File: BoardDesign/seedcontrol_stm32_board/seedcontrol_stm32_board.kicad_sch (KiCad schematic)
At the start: 3 parts, among them U1 STM32F401CCUx

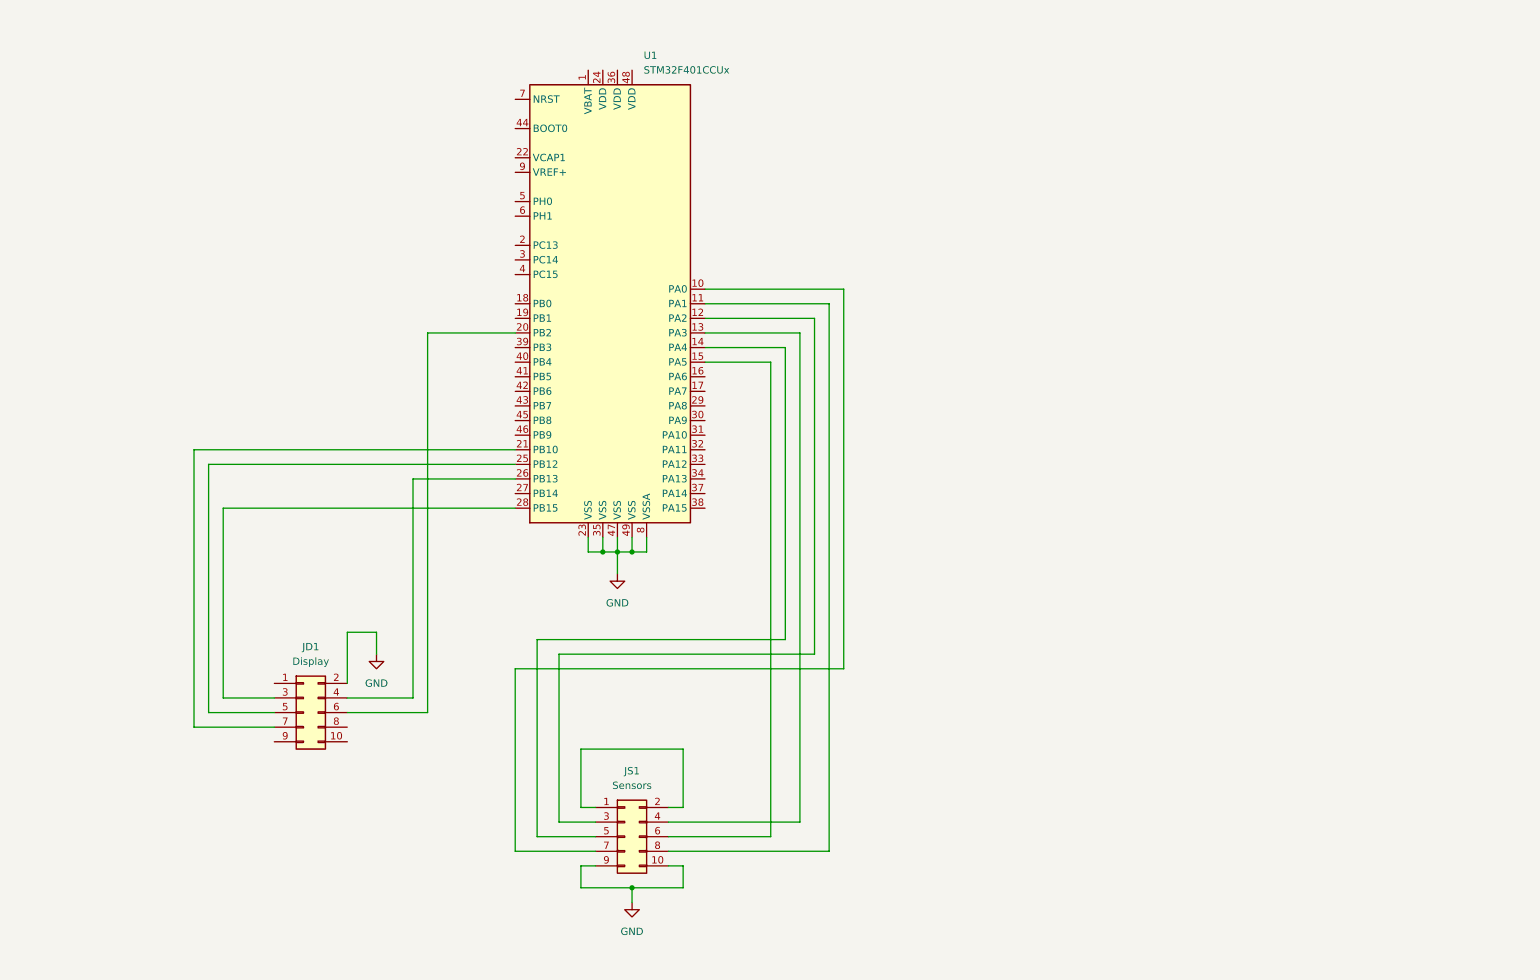
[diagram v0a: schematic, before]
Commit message: Added KiCAD schematic of the board and startet designing the PCB layout.
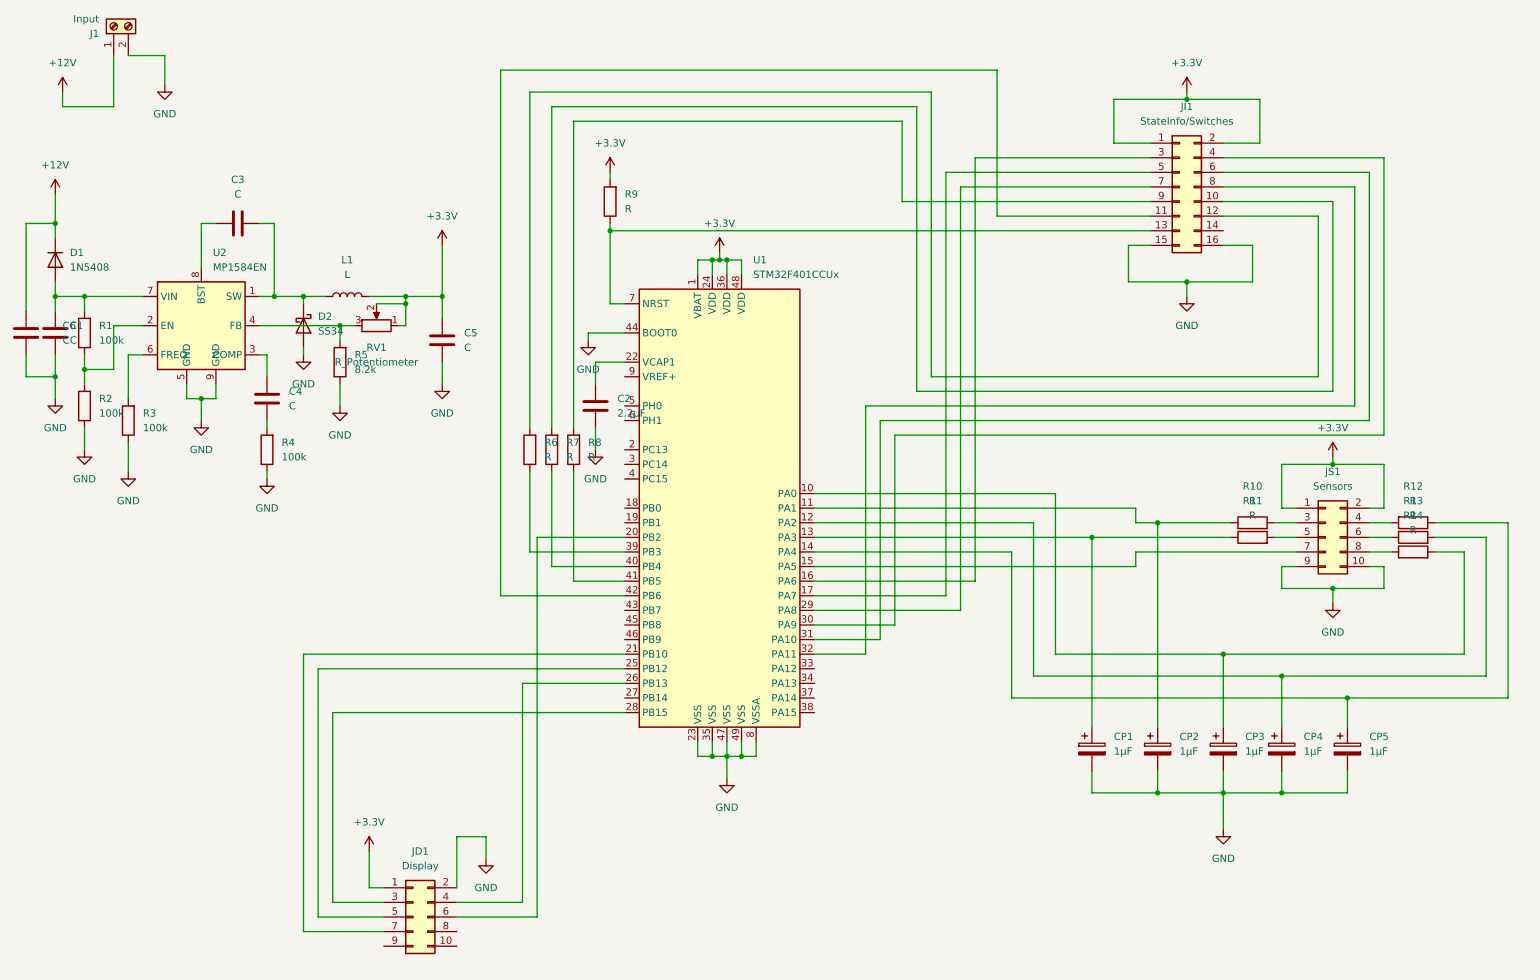
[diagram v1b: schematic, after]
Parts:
- added C1, C3, C4: C, Capacitor_SMD:C_0603_1608Metric, symbol Device:C
- added C2: 2.2µF, Capacitor_SMD:C_0402_1005Metric, symbol Device:C
- added C5, C6: C, Capacitor_SMD:C_1206_3216Metric, symbol Device:C
- added CP1, CP2, CP3, CP4, CP5: 1µF, Capacitor_THT:C_Rect_L10.0mm_W3.0mm_P7.50mm_MKS4, symbol Device:C_Polarized
- added D1: 1N5408, Diode_THT:D_DO-41_SOD81_P12.70mm_Horizontal, symbol Simulation_SPICE:DIODE
- added D2: SS34, Diode_SMD:D_SMC, symbol Device:D_Schottky
- added J1: Input, TerminalBlock:TerminalBlock_Altech_AK300-2_P5.00mm, symbol Connector:Screw_Terminal_01x02
- added JI1: StateInfo/Switches, Connector_PinHeader_2.54mm:PinHeader_2x08_P2.54mm_Vertical, symbol Connector_Generic:Conn_02x08_Odd_Even
- added L1: L, Inductor_SMD:L_Bourns_SRP7028A_7.3x6.6mm, symbol Device:L
- added R1, R2, R3, R4: 100k, Resistor_SMD:R_0603_1608Metric, symbol Device:R
- added R10, R11, R12, R13, R14: R, Resistor_THT:R_Axial_DIN0309_L9.0mm_D3.2mm_P12.70mm_Horizontal, symbol Device:R
- added R5: 8.2k, Resistor_SMD:R_0603_1608Metric, symbol Device:R
- added R6, R7, R8, R9: R, Resistor_SMD:R_0603_1608Metric, symbol Device:R
- added RV1: R_Potentiometer, Potentiometer_SMD:Potentiometer_Bourns_TC33X_Vertical, symbol Device_custom:R_Potentiometer
- added U2: MP1584EN, Package_SO:SOIC-8-1EP_3.9x4.9mm_P1.27mm_EP2.62x3.51mm, symbol Regulator_Switching_custom:MP1584EN
- JD1, JS1: footprint (none) -> Connector_PinHeader_2.54mm:PinHeader_2x05_P2.54mm_Vertical
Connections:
- net GND: now also U1.44 (BOOT0), C1.1, C2.1, C5.1, C6.1, CP1.2, CP2.2, CP3.2, CP4.2, CP5.2, D2.2 (A), J1.2 (Pin_2), JI1.15 (Pin_15), JI1.16 (Pin_16), R2.1, R3.1, R4.1, R5.1, U2.5 (GND), U2.9 (GND)
- net +3.3V: now reaches JS1.1 (Pin_1), JS1.2 (Pin_2)
- net +3.3V: now also JD1.1 (Pin_1), U1.1 (VBAT), U1.24 (VDD), U1.36 (VDD), U1.48 (VDD), C5.2, JI1.1 (Pin_1), JI1.2 (Pin_2), L1.2, R9.2, RV1.1, RV1.2
- net at U1.12 (PA2): now also CP4.1, R13.2; no longer JS1.3 (Pin_3)
- net at U1.13 (PA3): now also CP1.1, R11.1; no longer JS1.4 (Pin_4)
- net at JS1.5 (Pin_5): now also R11.2; no longer U1.14 (PA4)
- net at JS1.6 (Pin_6): now also R13.1; no longer U1.15 (PA5)
- net at U1.10 (PA0): now also CP3.1, R14.2; no longer JS1.7 (Pin_7)
- net at U1.11 (PA1): now also CP2.1, R10.1; no longer JS1.8 (Pin_8)
- net at U1.16 (PA6): now also JI1.3 (Pin_3)
- net at U1.17 (PA7): now also JI1.5 (Pin_5)
- net at U1.22 (VCAP1): now also C2.2
- net at U1.29 (PA8): now also JI1.7 (Pin_7)
- net at U1.30 (PA9): now also JI1.4 (Pin_4)
- net at U1.31 (PA10): now also JI1.6 (Pin_6)
- net at U1.32 (PA11): now also JI1.8 (Pin_8)
- net at U1.39 (PB3): now also R6.1
- net at U1.40 (PB4): now also R7.1
- net at U1.41 (PB5): now also R8.1
- net at U1.42 (PB6): now also JI1.11 (Pin_11)
- net at U1.7 (NRST): now also JI1.13 (Pin_13), R9.1
- new net: JI1.10 (Pin_10), R7.2
- new net: R5.2, RV1.3, U2.4 (FB)
- new net: C3.1, U2.8 (BST)
- new net: C3.2, D2.1 (K), L1.1, U2.1 (SW)
- new net: JI1.12 (Pin_12), R6.2
- new net: JI1.9 (Pin_9), R8.2
- new net: R1.1, R2.2, U2.2 (EN)
- new net: C4.2, U2.3 (COMP)
- new net: R3.2, U2.6 (FREQ)
- new net: C1.2, D1.1 (A), R1.2, U2.7 (VIN)
- new net: C4.1, R4.2
- new net: JS1.3 (Pin_3), R10.2
- new net: CP5.1, R12.1, U1.14 (PA4)
- new net: JS1.4 (Pin_4), R12.2
- new net: JS1.8 (Pin_8), R14.1
- new net: JS1.7 (Pin_7), U1.15 (PA5)
- new net +12V: C6.2, D1.2 (K), J1.1 (Pin_1)
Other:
- moved on the sheet: JD1, U1

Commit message: Finalized board layout.
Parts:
- added JP1: Programming, Connector_PinHeader_2.54mm:PinHeader_2x05_P2.54mm_Vertical, symbol Connector_Generic:Conn_02x05_Odd_Even
- JI1: value StateInfo/Switches -> Info/Switches
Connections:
- net +3.3V: now also JP1.4 (Pin_4)
- net GND: now also JP1.2 (Pin_2)
- net at U1.34 (PA13): now also JP1.3 (Pin_3)
- net at U1.37 (PA14): now also JP1.1 (Pin_1)

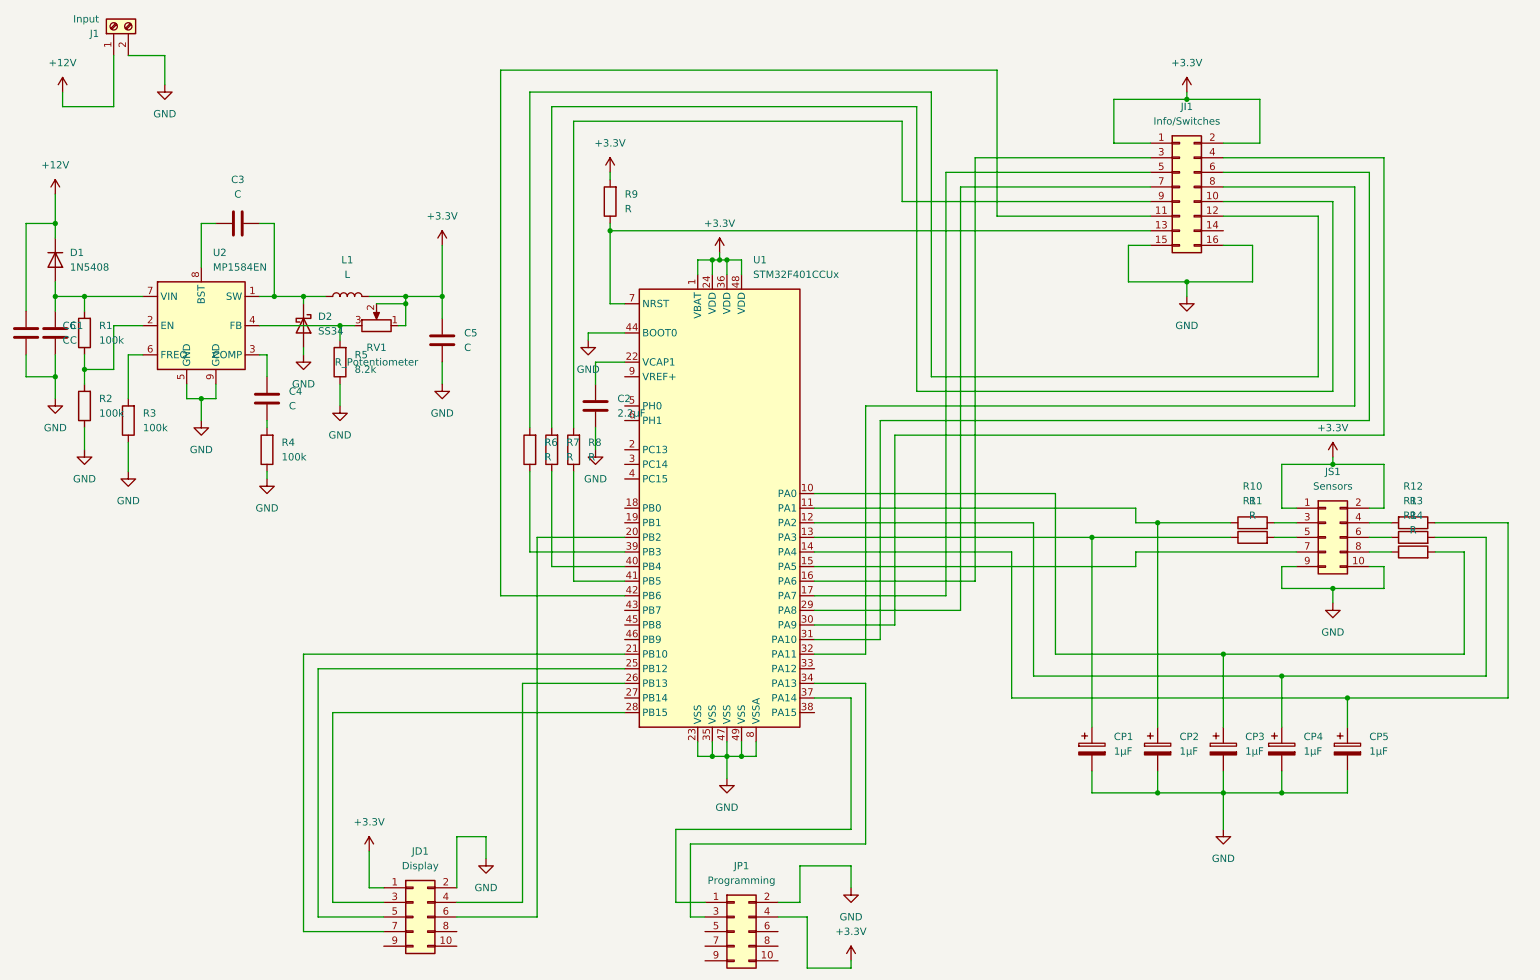
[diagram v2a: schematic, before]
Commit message: Changed board design. Added footprint for STM32_Blackpill connector.
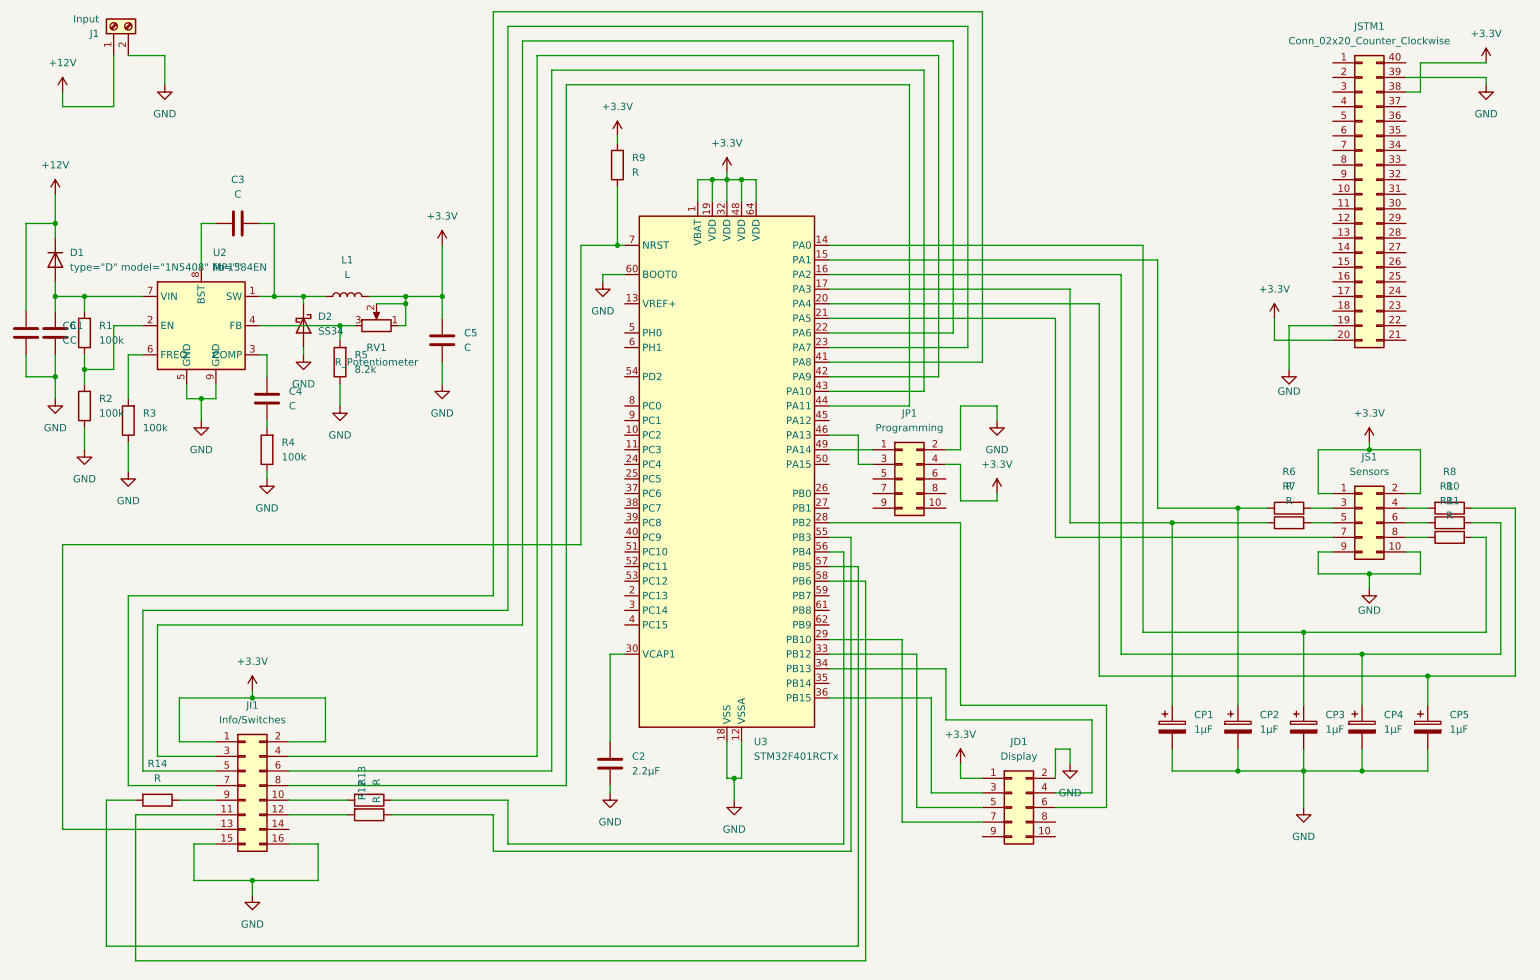
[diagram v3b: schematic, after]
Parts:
- removed U1: STM32F401CCUx, Package_DFN_QFN:QFN-48-1EP_7x7mm_P0.5mm_EP5.6x5.6mm, symbol MCU_ST_STM32F4:STM32F401CCUx
- added JSTM1: Conn_02x20_Counter_Clockwise, custom:STM32_Blackpill_header, symbol Connector_Generic:Conn_02x20_Counter_Clockwise
- added U3: STM32F401RCTx, Package_QFP:LQFP-64_10x10mm_P0.5mm, symbol MCU_ST_STM32F4:STM32F401RCTx
- D1: value 1N5408 -> ${SIM.PARAMS}; Spice_Netlist_Enabled Y -> (none); Spice_Primitive D -> (none)
- R12, R13, R14: footprint Resistor_THT:R_Axial_DIN0309_L9.0mm_D3.2mm_P12.70mm_Horizontal -> Resistor_SMD:R_0603_1608Metric
- R6, R7, R8: footprint Resistor_SMD:R_0603_1608Metric -> Resistor_THT:R_Axial_DIN0309_L9.0mm_D3.2mm_P12.70mm_Horizontal
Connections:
- net +3.3V: now also JSTM1.20 (Pin_20), JSTM1.38 (Pin_38), U3.1 (VBAT), U3.19 (VDD), U3.32 (VDD), U3.48 (VDD), U3.64 (VDD)
- net GND: now also JSTM1.19 (Pin_19), JSTM1.39 (Pin_39), U3.12 (VSSA), U3.18 (VSS), U3.31 (VSS), U3.47 (VSS), U3.60 (BOOT0), U3.63 (VSS)
- net at R7.1: now also CP1.1, U3.17 (PA3)
- net at JI1.10 (Pin_10): now also R13.2; no longer R7.2
- net at R11.1: now also JS1.8 (Pin_8); no longer CP1.1
- net at R11.2: now also CP3.1, U3.14 (PA0); no longer JS1.5 (Pin_5)
- net at C2.2: now also U3.30 (VCAP1)
- net at JI1.11 (Pin_11): now also U3.58 (PB6)
- net at JI1.12 (Pin_12): now also R12.2; no longer R6.2
- net at JI1.13 (Pin_13), R9.1: now also U3.7 (NRST)
- net at JI1.3 (Pin_3): now also U3.22 (PA6)
- net at JI1.4 (Pin_4): now also U3.42 (PA9)
- net at JI1.5 (Pin_5): now also U3.23 (PA7)
- net at JI1.6 (Pin_6): now also U3.43 (PA10)
- net at JI1.7 (Pin_7): now also U3.41 (PA8)
- net at JI1.8 (Pin_8): now also U3.44 (PA11)
- net at JI1.9 (Pin_9): now also R14.1; no longer R8.2
- net at R13.1: now also U3.56 (PB4); no longer JS1.6 (Pin_6)
- net at CP4.1: now also R10.2, U3.16 (PA2); no longer R13.2
- net at CP2.1: now also R6.1, U3.15 (PA1); no longer R10.1
- net at JS1.3 (Pin_3): now also R6.2; no longer R10.2
- net at R14.2: now also U3.57 (PB5); no longer CP3.1
- net at CP5.1: now also R8.1, U3.20 (PA4); no longer R12.1
- net at JS1.4 (Pin_4): now also R8.2; no longer R12.2
- net at JP1.1 (Pin_1): now also U3.49 (PA14)
- net at JP1.3 (Pin_3): now also U3.46 (PA13)
- net at JS1.7 (Pin_7): now also U3.21 (PA5)
- net at JD1.6 (Pin_6): now also U3.28 (PB2)
- net at JD1.7 (Pin_7): now also U3.29 (PB10)
- net at JD1.5 (Pin_5): now also U3.33 (PB12)
- net at JD1.4 (Pin_4): now also U3.34 (PB13)
- net at JD1.3 (Pin_3): now also U3.36 (PB15)
- new net: R12.1, U3.55 (PB3)
- new net: JS1.5 (Pin_5), R7.2
- new net: JS1.6 (Pin_6), R10.1
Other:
- moved on the sheet: C2, R9
